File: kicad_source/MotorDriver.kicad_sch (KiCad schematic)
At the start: 44 parts, among them J7 x, J8 x, J9 x, Q1 2N7002, U4 74xx08, U5 IFX007T, U6 IFX007T, U7 IFX007T, U8 IFX007T

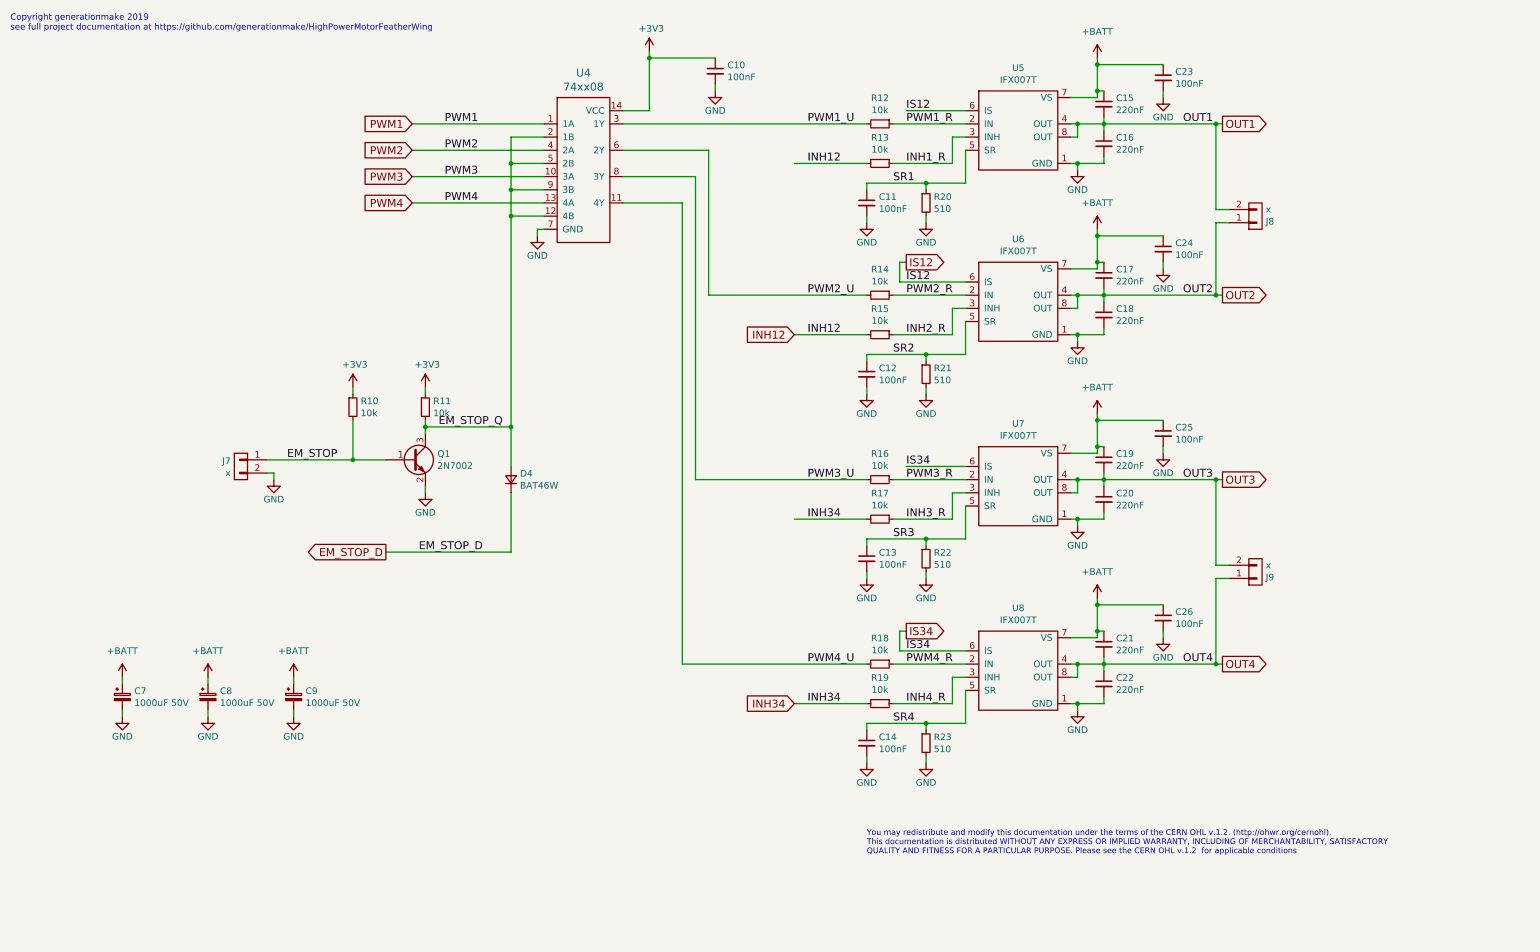
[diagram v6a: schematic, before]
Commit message: updated schematic pdf
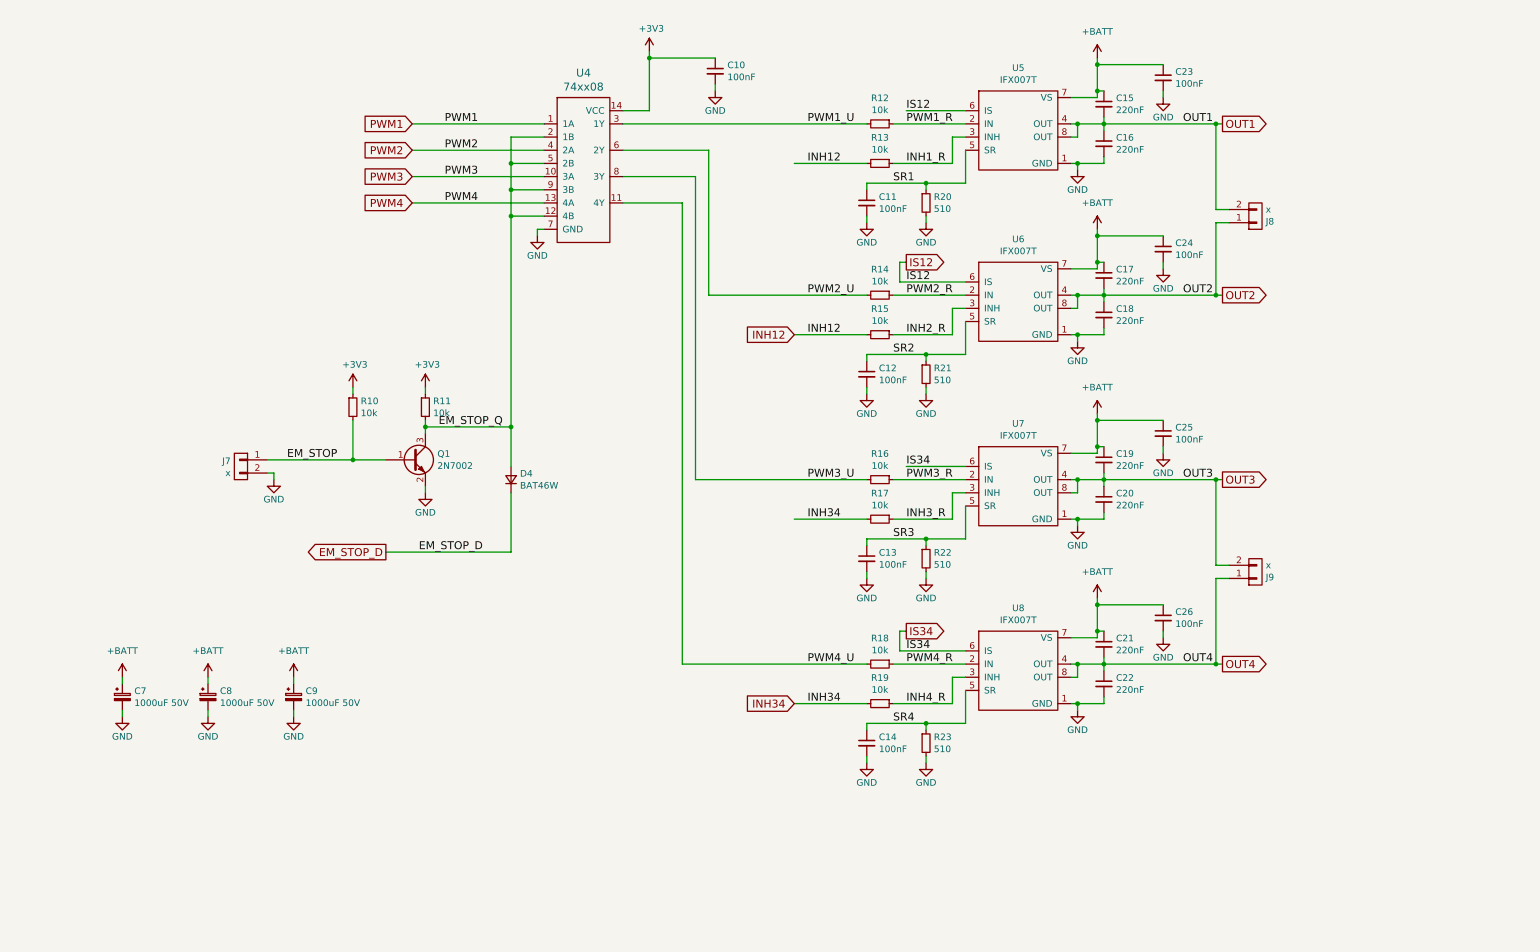
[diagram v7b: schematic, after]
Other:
- note removed: "Copyright generationmake 2019 see full project documentation at https://github.com/generationmake/HighPowerMotorFeatherWing"
- note removed: "You may redistribute and modify this documentation under the terms of the CERN OHL v.1.2. (http://ohwr.org/cernohl). This documentation is distributed WITHOUT ANY EXPRESS OR IMPLIED WARRANTY, INCLUDING OF MERCHANTABILITY, SATISFACTORY QUALITY AND FITNESS FOR A PARTICULAR PURPOSE. Please see the CERN OHL v.1.2 for applicable conditions"
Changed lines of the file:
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@@
   (title_block
     (title "CyphalRobotController07/CAN")
-    (date "2023-10-01")
+    (date "2023-10-02")
     (rev "0.1")
     (company "generationmake")
@@
     (stroke (width 0) (type default) (color 0 0 0 0))
   )
-  (text "You may redistribute and modify this documentation under the terms of the CERN OHL v.1.2. (http://ohwr.org/cernohl). \nThis documentation is distributed WITHOUT ANY EXPRESS OR IMPLIED WARRANTY, INCLUDING OF MERCHANTABILITY, SATISFACTORY \nQUALITY AND FITNESS FOR A PARTICULAR PURPOSE. Please see the CERN OHL v.1.2  for applicable conditions"
-    (at 177.8 175.26 0)
-    (effects (font (size 1.0922 1.0922)) (justify left bottom))
-  )
-  (text "Copyright generationmake 2019\nsee full project documentation at https://github.com/generationmake/HighPowerMotorFeatherWing"
-    (at 12.7 16.51 0)
-    (effects (font (size 1.1938 1.1938)) (justify left bottom))
-  )
   (label "PWM2_U" (at 166.37 67.31 0)

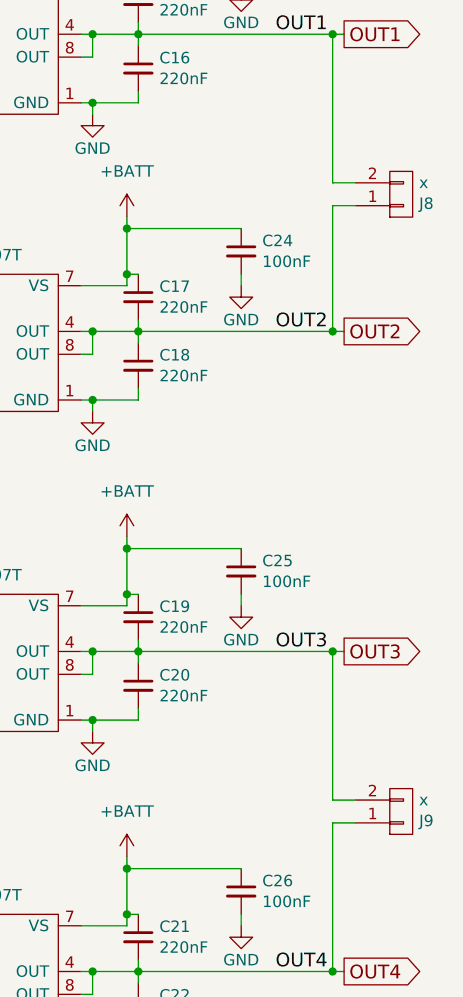
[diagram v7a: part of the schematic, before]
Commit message: updated 3d model to fit to reality
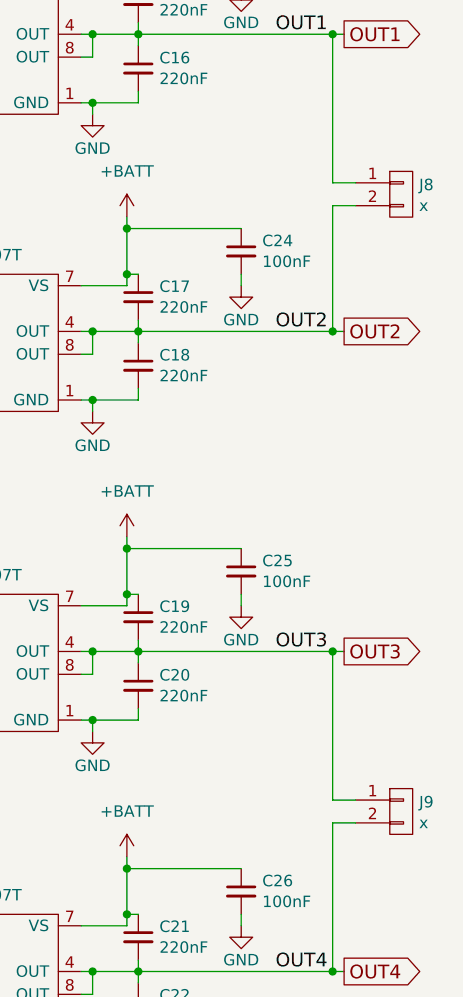
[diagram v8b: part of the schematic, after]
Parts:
- J8, J9: footprint Connector_Phoenix_MC:PhoenixContact_MCV_1,5_2-G-3.81_1x02_P3.81mm_Vertical -> Connector_Phoenix_MC:PhoenixContact_MC_1,5_2-G-3.81_1x02_P3.81mm_Horizontal
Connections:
- net OUT1: now also J8.1 (P1); no longer J8.2 (P2)
- net OUT2: now also J8.2 (P2); no longer J8.1 (P1)
- net OUT3: now also J9.1 (P1); no longer J9.2 (P2)
- net OUT4: now also J9.2 (P2); no longer J9.1 (P1)
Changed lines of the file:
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@@
   (title_block
     (title "CyphalRobotController07/CAN")
-    (date "2023-10-02")
+    (date "2023-11-15")
     (rev "0.1")
     (company "generationmake")
@@
     )
   )
-  (symbol (lib_id "OpenCyphalRobotController07-rescue:WR-TBL_691313710002-mechanical-connectors") (at 252.73 52.07 0) (mirror x) (unit 1)
+  (symbol (lib_id "OpenCyphalRobotController07-rescue:WR-TBL_691313710002-mechanical-connectors") (at 252.73 52.07 0) (unit 1)
     (in_bom yes) (on_board yes)
-    (property "Reference" "J8" (id 0) (at 254.7112 53.1114 0)
+    (property "Reference" "J8" (id 0) (at 254.7112 51.0286 0)
       (effects (font (size 1.27 1.27)) (justify left))
     )
-    (property "Value" "x" (id 1) (at 254.7112 50.8 0)
+    (property "Value" "x" (id 1) (at 254.7112 53.34 0)
       (effects (font (size 1.27 1.27)) (justify left))
     )
-    (property "Footprint" "Connector_Phoenix_MC:PhoenixContact_MCV_1,5_2-G-3.81_1x02_P3.81mm_Vertical" (id 2) (at 250.19 53.34 0)
+    (property "Footprint" "Connector_Phoenix_MC:PhoenixContact_MC_1,5_2-G-3.81_1x02_P3.81mm_Horizontal" (id 2) (at 250.19 50.8 0)
       (effects (font (size 1.27 1.27)) hide)
     )
@@
     (pin "2")
   )
-  (symbol (lib_id "OpenCyphalRobotController07-rescue:WR-TBL_691313710002-mechanical-connectors") (at 252.73 120.65 0) (mirror x) (unit 1)
+  (symbol (lib_id "OpenCyphalRobotController07-rescue:WR-TBL_691313710002-mechanical-connectors") (at 252.73 120.65 0) (unit 1)
     (in_bom yes) (on_board yes)
-    (property "Reference" "J9" (id 0) (at 254.7112 121.6914 0)
+    (property "Reference" "J9" (id 0) (at 254.7112 119.6086 0)
       (effects (font (size 1.27 1.27)) (justify left))
     )
-    (property "Value" "x" (id 1) (at 254.7112 119.38 0)
+    (property "Value" "x" (id 1) (at 254.7112 121.92 0)
       (effects (font (size 1.27 1.27)) (justify left))
     )
-    (property "Footprint" "Connector_Phoenix_MC:PhoenixContact_MCV_1,5_2-G-3.81_1x02_P3.81mm_Vertical" (id 2) (at 250.19 121.92 0)
-      (effects (font (size 1.27 1.27)) hide)
-    )
+    (property "Footprint" "Connector_Phoenix_MC:PhoenixContact_MC_1,5_2-G-3.81_1x02_P3.81mm_Horizontal" (id 2) (at 250.19 119.38 0)
+      (effects (font (size 1.27 1.27)) hide)
+    )
